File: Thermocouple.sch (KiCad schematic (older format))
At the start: 0 parts

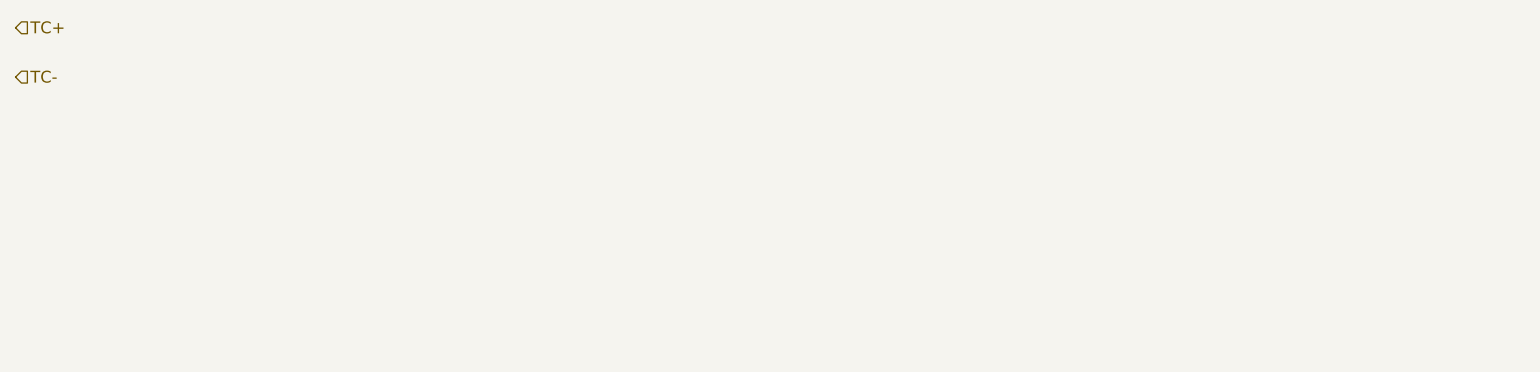
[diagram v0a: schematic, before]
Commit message: Added pins to sheets of block diagram.
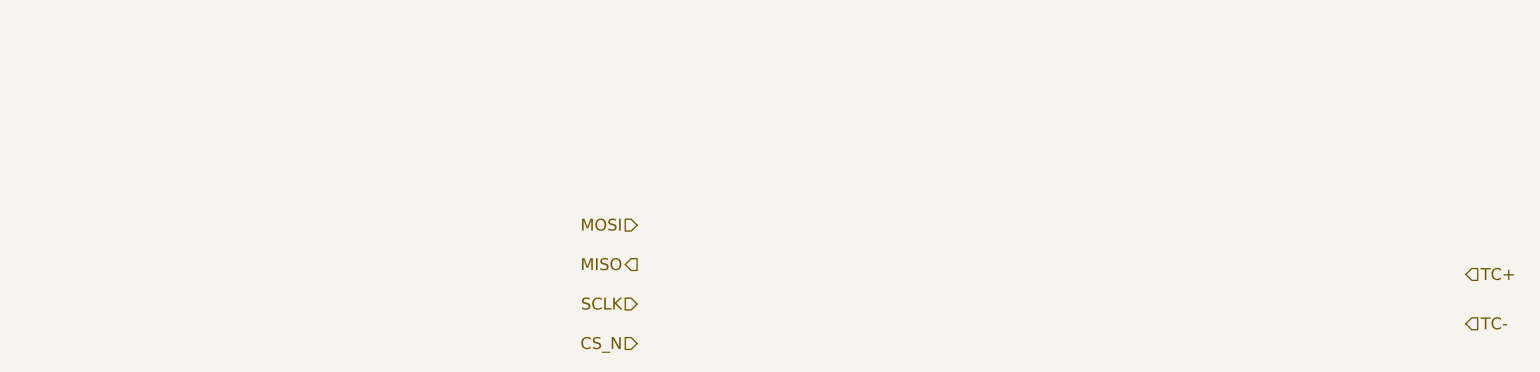
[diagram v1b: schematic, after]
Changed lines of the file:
@@
-EESchema Schematic File Version 2  date Tue 04 Feb 2014 11:04:27 PM EST
+EESchema Schematic File Version 2  date Tue 04 Feb 2014 11:45:57 PM EST
 LIBS:power
 LIBS:device
@@
 Comment4 ""
 $EndDescr
-Text HLabel 2250 2050 2    60   Input ~ 0
+Text HLabel 5400 3400 0    60   Input ~ 0
+CS_N
+Text HLabel 5400 3200 0    60   Input ~ 0
+SCLK
+Text HLabel 5400 3000 0    60   Output ~ 0
+MISO
+Text HLabel 5400 2800 0    60   Input ~ 0
+MOSI
+Text HLabel 9600 3300 2    60   Input ~ 0
 TC-
-Text HLabel 2250 1800 2    60   Input ~ 0
+Text HLabel 9600 3050 2    60   Input ~ 0
 TC+
 $EndSCHEMATC

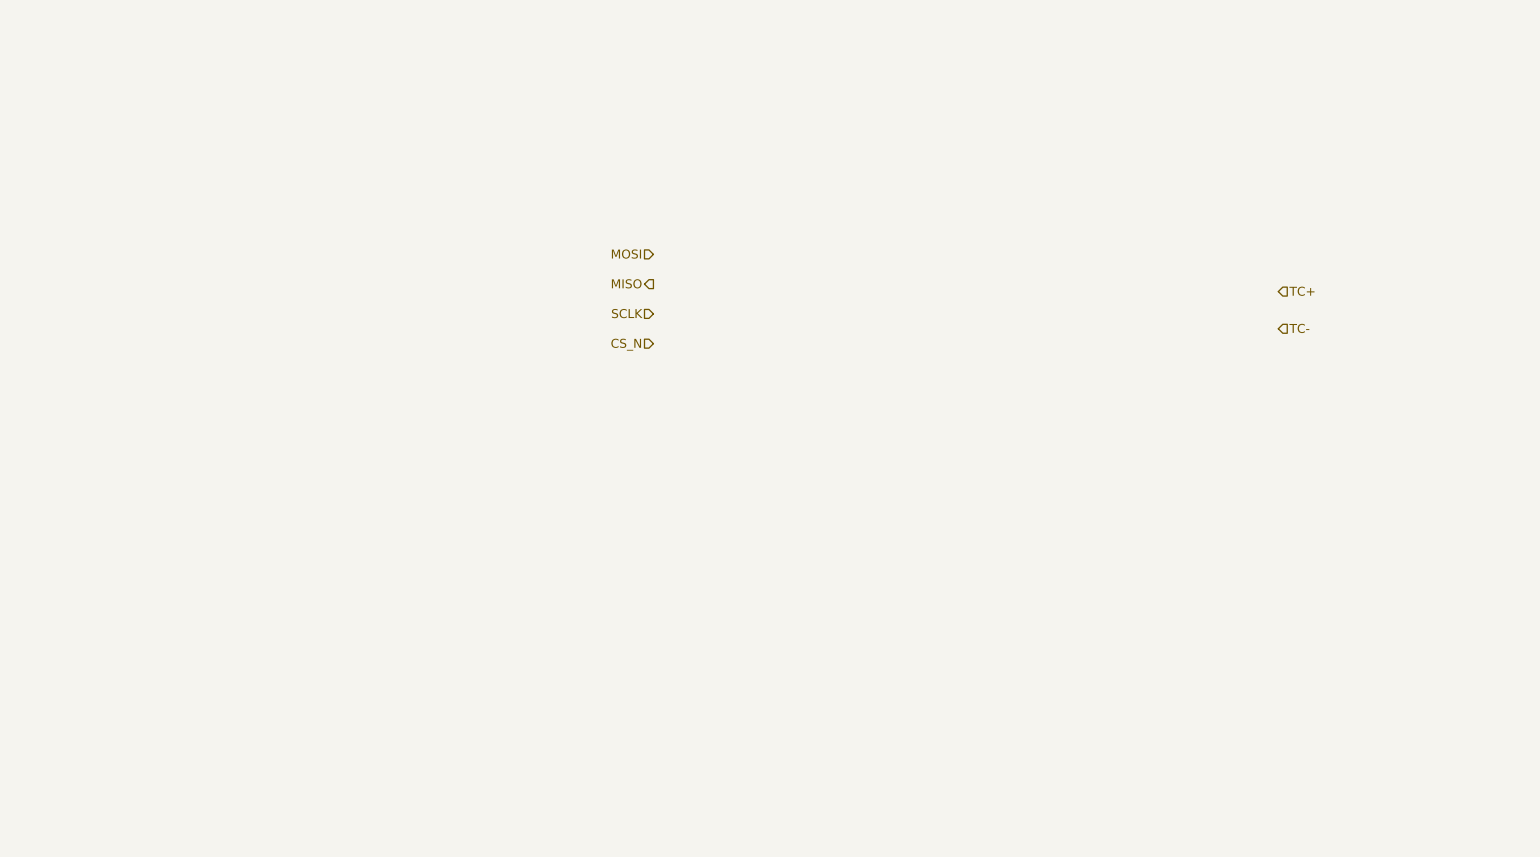
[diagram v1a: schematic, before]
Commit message: Detailed out Thermocouple sheet
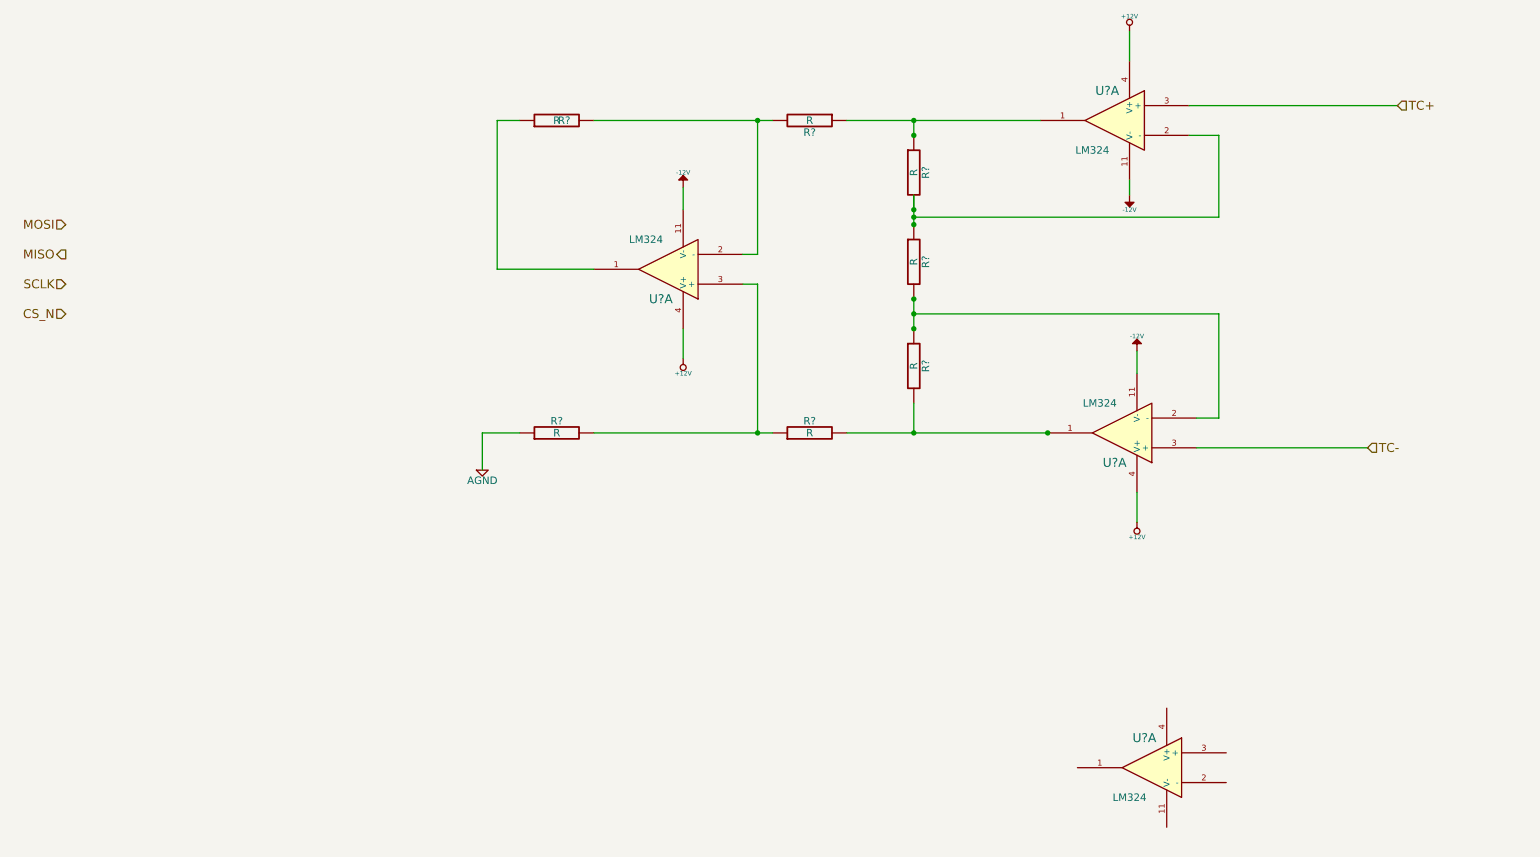
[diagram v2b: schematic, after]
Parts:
- added R? (x7): R, symbol R
- added U? (x4): LM324, symbol LM324
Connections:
- net TC+: now also U?.3 (+)
- net TC-: now also U?.3 (+)
- new net: R?.1, R?.1, U?.1
- new net: R?.1, R?.2, U?.2 (-) (x2)
- new net: R?.2, R?.2, U?.1
- new net: R?.1, U?.1
- new net: R?.2, R?.2, U?.2 (-)
- new net: R?.1, R?.2, U?.3 (+)
- new net +12V: U?.4 (V+), U?.4 (V+), U?.4 (V+)
- new net -12V: U?.11 (V-), U?.11 (V-), U?.11 (V-)
- new net AGND: R?.1

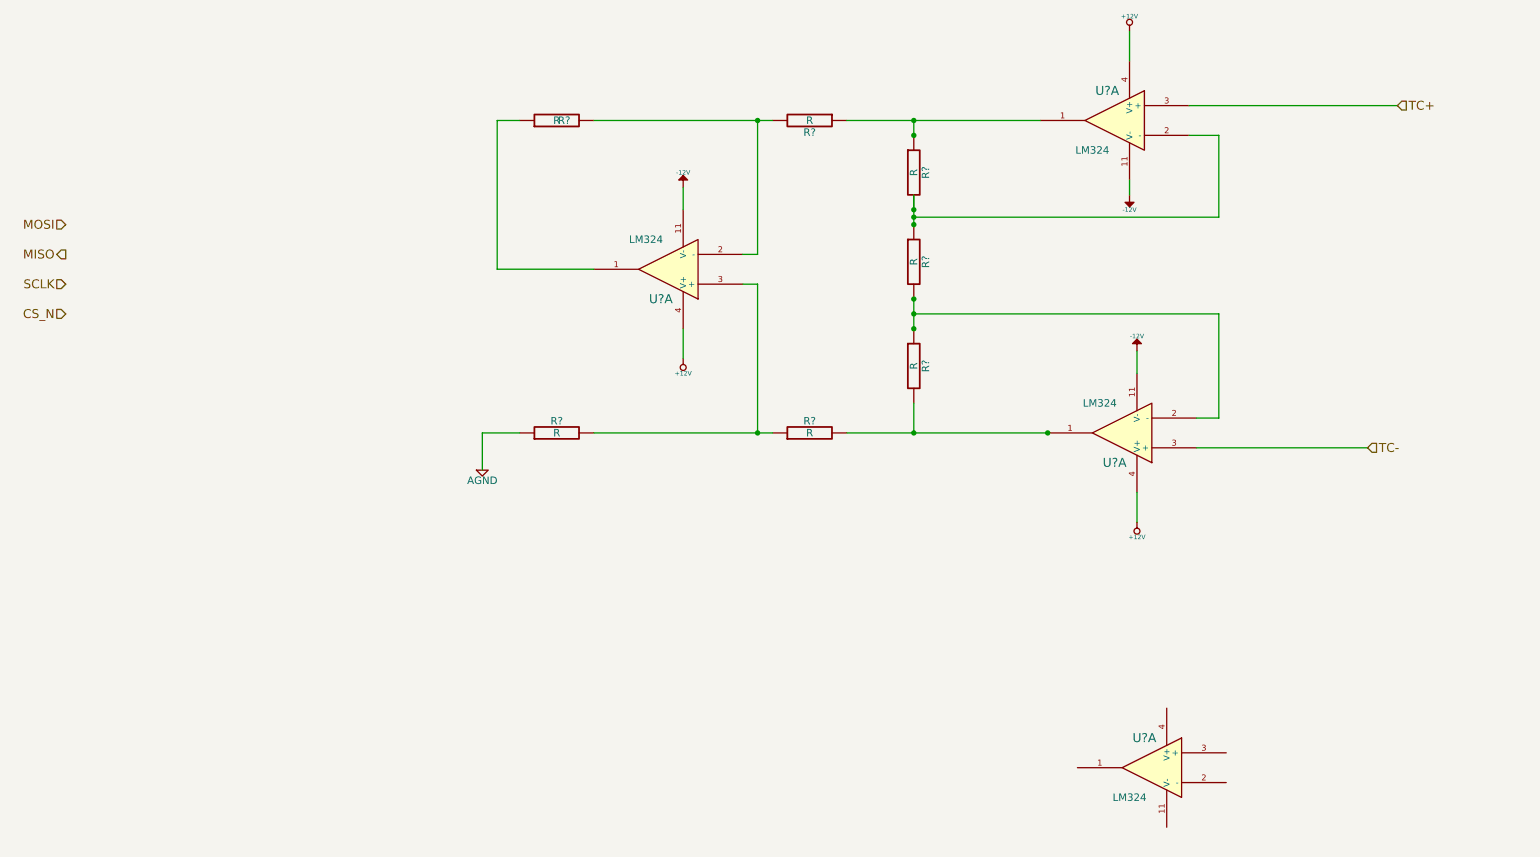
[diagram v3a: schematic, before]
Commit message: Updated with correct DAC and ADC for thermo and fan
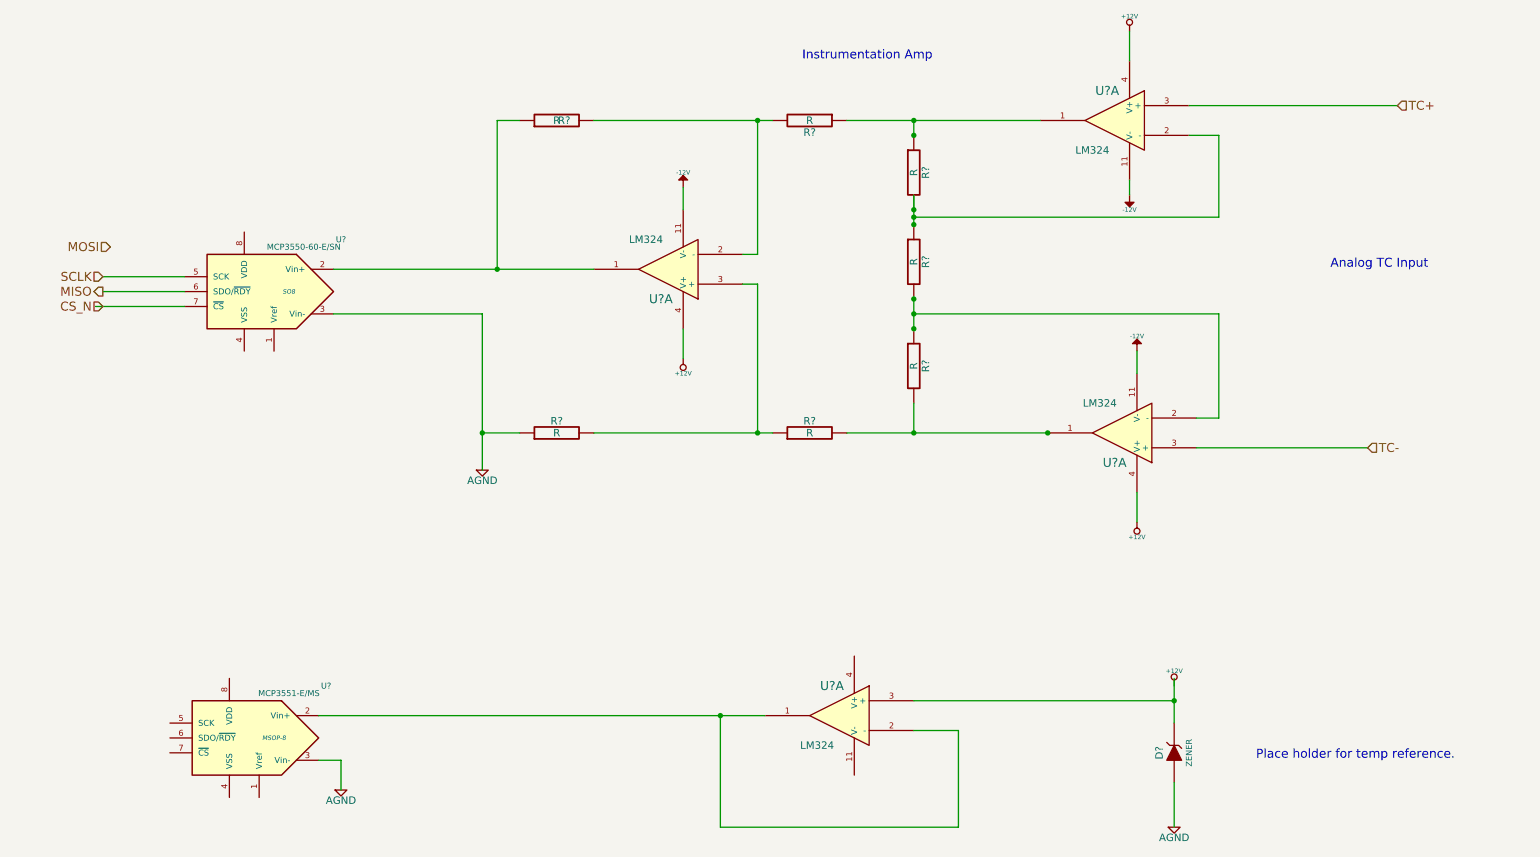
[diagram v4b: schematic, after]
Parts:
- added D?: ZENER, ~, symbol ZENER
- added U?: MCP3551-E/MS, MSOP-8, symbol MCP3551-E/MS
- added U?: MCP3550-60-E/SN, SO8, symbol MCP3550-60-E/SN
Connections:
- wire segments 31 -> 45
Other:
- note added: "Analog TC Input"
- note added: "Instrumentation Amp"
- note added: "Place holder for temp reference."
- moved on the sheet: U?A
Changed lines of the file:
@@
-EESchema Schematic File Version 2  date Thu 06 Feb 2014 12:03:55 AM EST
+EESchema Schematic File Version 2
 LIBS:power
 LIBS:device
@@
 LIBS:valves
 LIBS:InitialKiCadProject-cache
-EELAYER 25  0
+EELAYER 27 0
 EELAYER END
-$Descr A4 11700 8267
+$Descr A4 11693 8268
 encoding utf-8
 Sheet 7 8
 Title ""
-Date "6 feb 2014"
+Date "7 feb 2014"
 Rev ""
 Comp ""
@@
 $EndDescr
 Wire Wire Line
-	4250 4250 4250 4000
+	4250 3200 4250 4250
 Wire Wire Line
 	4250 4000 4500 4000
@@
 	6100 2800 6000 2800
 Wire Wire Line
-	5000 2900 4350 2900
+	3250 2900 5000 2900
 Wire Wire Line
 	4350 2900 4350 1900
@@
 F 0 "#PWR?" H 4250 4250 40  0001 C CNN
 F 1 "AGND" H 4250 4180 50  0000 C CNN
+F 2 "" H 4250 4250 60  0001 C CNN
+F 3 "" H 4250 4250 60  0001 C CNN
 	1    4250 4250
 	1    0    0    -1
@@
 F 0 "#PWR?" H 5600 3450 20  0001 C CNN
 F 1 "+12V" H 5600 3600 30  0000 C CNN
+F 2 "" H 5600 3500 60  0001 C CNN
+F 3 "" H 5600 3500 60  0001 C CNN
 	1    5600 3500
 	1    0    0    1
@@
 F 0 "#PWR?" H 8650 4550 20  0001 C CNN
 F 1 "+12V" H 8650 4700 30  0000 C CNN
+F 2 "" H 8650 4600 60  0001 C CNN
+F 3 "" H 8650 4600 60  0001 C CNN
 	1    8650 4600
 	1    0    0    1
@@
 F 0 "#PWR?" H 8600 1250 20  0001 C CNN
 F 1 "+12V" H 8600 1400 30  0000 C CNN
+F 2 "" H 8600 1300 60  0001 C CNN
+F 3 "" H 8600 1300 60  0001 C CNN
 	1    8600 1300
 	1    0    0    -1
@@
 F 0 "#PWR?" H 8650 3580 20  0001 C CNN
 F 1 "-12V" H 8650 3550 30  0000 C CNN
+F 2 "" H 8650 3450 60  0001 C CNN
+F 3 "" H 8650 3450 60  0001 C CNN
 	1    8650 3450
 	1    0    0    -1
@@
 F 0 "#PWR?" H 8600 2530 20  0001 C CNN
 F 1 "-12V" H 8600 2500 30  0000 C CNN
+F 2 "" H 8600 2400 60  0001 C CNN
+F 3 "" H 8600 2400 60  0001 C CNN
 	1    8600 2400
 	1    0    0    1
@@
 F 0 "#PWR?" H 5600 2480 20  0001 C CNN
 F 1 "-12V" H 5600 2450 30  0000 C CNN
+F 2 "" H 5600 2350 60  0001 C CNN
+F 3 "" H 5600 2350 60  0001 C CNN
 	1    5600 2350
 	1    0    0    -1
@@
 F 0 "R?" V 6530 1900 50  0000 C CNN
 F 1 "R" V 6450 1900 50  0000 C CNN
+F 2 "" H 6450 1900 60  0001 C CNN
+F 3 "" H 6450 1900 60  0001 C CNN
 	1    6450 1900
 	0    1    1    0
@@
 F 0 "R?" V 4750 1850 50  0000 C CNN
 F 1 "R" V 4750 1900 50  0000 C CNN
+F 2 "" H 4750 1900 60  0001 C CNN
+F 3 "" H 4750 1900 60  0001 C CNN
 	1    4750 1900
 	0    -1   -1   0
@@
 F 0 "R?" V 4830 4000 50  0000 C CNN
 F 1 "R" V 4750 4000 50  0000 C CNN
+F 2 "" H 4750 4000 60  0001 C CNN
+F 3 "" H 4750 4000 60  0001 C CNN
 	1    4750 4000
 	0    -1   -1   0
@@
 F 0 "R?" V 6530 4000 50  0000 C CNN
 F 1 "R" V 6450 4000 50  0000 C CNN
+F 2 "" H 6450 4000 60  0001 C CNN
+F 3 "" H 6450 4000 60  0001 C CNN
 	1    6450 4000
 	0    -1   -1   0
@@
 F 0 "R?" V 7230 3550 50  0000 C CNN
 F 1 "R" V 7150 3550 50  0000 C CNN
+F 2 "" H 7150 3550 60  0001 C CNN
+F 3 "" H 7150 3550 60  0001 C CNN
 	1    7150 3550
 	1    0    0    -1
@@
 F 0 "R?" V 7230 2850 50  0000 C CNN
 F 1 "R" V 7150 2850 50  0000 C CNN
+F 2 "" H 7150 2850 60  0001 C CNN
+F 3 "" H 7150 2850 60  0001 C CNN
 	1    7150 2850
 	1    0    0    -1
@@
 F 0 "R?" V 7230 2250 50  0000 C CNN
 F 1 "R" V 7150 2250 50  0000 C CNN
+F 2 "" H 7150 2250 60  0001 C CNN
+F 3 "" H 7150 2250 60  0001 C CNN
 	1    7150 2250
 	1    0    0    -1
@@
 L LM324 U?
 U 1 1 52F1C9D7
-P 8750 6250
-F 0 "U?" H 8800 6450 60  0000 C CNN
-F 1 "LM324" H 8900 6050 50  0000 C CNN
-	1    8750 6250
+P 6650 5900
+F 0 "U?" H 6700 6100 60  0000 C CNN
+F 1 "LM324" H 6800 5700 50  0000 C CNN
+F 2 "" H 6650 5900 60  0001 C CNN
+F 3 "" H 6650 5900 60  0001 C CNN
+	1    6650 5900
 	-1   0    0    -1
 $EndComp
@@
 F 0 "U?" H 5550 3100 60  0000 C CNN
 F 1 "LM324" H 5650 2700 50  0000 C CNN
+F 2 "" H 5500 2900 60  0001 C CNN
+F 3 "" H 5500 2900 60  0001 C CNN
 	1    5500 2900
 	-1   0    0    1
@@
 F 0 "U?" H 8600 4200 60  0000 C CNN
 F 1 "LM324" H 8700 3800 50  0000 C CNN
+F 2 "" H 8550 4000 60  0001 C CNN
+F 3 "" H 8550 4000 60  0001 C CNN
 	1    8550 4000
 	-1   0    0    1
@@
 F 0 "U?" H 8550 2100 60  0000 C CNN
 F 1 "LM324" H 8650 1700 50  0000 C CNN
+F 2 "" H 8500 1900 60  0001 C CNN
+F 3 "" H 8500 1900 60  0001 C CNN
 	1    8500 1900
 	-1   0    0    -1
 $EndComp
-Text HLabel 1450 3200 0    60   Input ~ 0
+Text HLabel 1700 3150 0    60   Input ~ 0
 CS_N
-Text HLabel 1450 3000 0    60   Input ~ 0
+Text HLabel 1700 2950 0    60   Input ~ 0
 SCLK
-Text HLabel 1450 2800 0    60   Output ~ 0
+Text HLabel 1700 3050 0    60   Output ~ 0
 MISO
-Text HLabel 1450 2600 0    60   Input ~ 0
+Text HLabel 1750 2750 0    60   Input ~ 0
 MOSI
 Text HLabel 10200 4100 2    60   Input ~ 0
@@
 Text HLabel 10400 1800 2    60   Input ~ 0
 TC+
+Wire Wire Line
+	1700 2950 2250 2950
+Wire Wire Line
+	1700 3050 2250 3050
+Wire Wire Line
+	1650 3150 2250 3150
+Connection ~ 4350 2900
+Wire Wire Line
+	4250 3200 3250 3200
+Connection ~ 4250 4000
+$Comp
+L MCP3551-E/MS U?
+U 1 1 52F43A87
+P 2650 6050
+F 0 "U?" H 2100 6400 40  0000 C CNN
+F 1 "MCP3551-E/MS" H 2350 6350 40  0000 C CNN
+F 2 "MSOP-8" H 2450 6050 30  0000 C CIN
+F 3 "" H 2650 6050 60  0000 C CNN
+	1    2650 6050
+	-1   0    0    -1
+$EndComp
+$Comp
+L ZENER D?
+U 1 1 52F43A99
+P 8900 6150
+F 0 "D?" H 8900 6250 50  0000 C CNN
+F 1 "ZENER" H 8900 6050 40  0000 C CNN
+F 2 "~" H 8900 6150 60  0000 C CNN
+F 3 "~" H 8900 6150 60  0000 C CNN
+	1    8900 6150
+	0    -1   -1   0
+$EndComp
+$Comp
+L +12V #PWR?
+U 1 1 52F43AAD
+P 8900 5700
+F 0 "#PWR?" H 8900 5650 20  0001 C CNN
+F 1 "+12V" H 8900 5800 30  0000 C CNN
+F 2 "" H 8900 5700 60  0000 C CNN
+F 3 "" H 8900 5700 60  0000 C CNN
+	1    8900 5700
+	1    0    0    -1
+$EndComp
+Wire Wire Line
+	8900 5650 8900 5950
+$Comp
+L AGND #PWR?
+U 1 1 52F43AEC
+P 8900 6650
+F 0 "#PWR?" H 8900 6650 40  0001 C CNN
+F 1 "AGND" H 8900 6580 50  0000 C CNN
+F 2 "" H 8900 6650 60  0001 C CNN
+F 3 "" H 8900 6650 60  0001 C CNN
+	1    8900 6650
+	1    0    0    -1
+$EndComp
+Wire Wire Line
+	8900 6350 8900 6650
+Text Notes 9450 6200 0    60   ~ 0
+Place holder for temp reference.
+Text Notes 9950 2900 0    60   ~ 0
+Analog TC Input
+Text Notes 6400 1500 0    60   ~ 0
+Instrumentation Amp
+Wire Wire Line
+	7150 5800 8900 5800
+Connection ~ 8900 5800
+Wire Wire Line
+	3150 5900 6150 5900
+Wire Wire Line
+	7150 6000 7450 6000
+Wire Wire Line
+	7450 6000 7450 6650
+Wire Wire Line
+	7450 6650 5850 6650
+Wire Wire Line
+	5850 6650 5850 5900
+Connection ~ 5850 5900
+$Comp
+L AGND #PWR?
+U 1 1 52F43C09
+P 3300 6400
+F 0 "#PWR?" H 3300 6400 40  0001 C CNN
+F 1 "AGND" H 3300 6330 50  0000 C CNN
+F 2 "" H 3300 6400 60  0001 C CNN
+F 3 "" H 3300 6400 60  0001 C CNN
+	1    3300 6400
+	1    0    0    -1
+$EndComp
+Wire Wire Line
+	3150 6200 3300 6200
+Wire Wire Line
+	3300 6200 3300 6400
+$Comp
+L MCP3550-60-E/SN U?
+U 1 1 52F445A3
+P 2750 3050
+F 0 "U?" H 2200 3400 40  0000 C CNN
+F 1 "MCP3550-60-E/SN" H 2450 3350 40  0000 C CNN
+F 2 "SO8" H 2550 3050 30  0000 C CIN
+F 3 "" H 2750 3050 60  0000 C CNN
+	1    2750 3050
+	-1   0    0    -1
+$EndComp
 $EndSCHEMATC
